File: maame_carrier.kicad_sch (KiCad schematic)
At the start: 30 parts, among them J1 To Kakute H7 V1.5: left strip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, J10 FS-iA10B iBUS servo lead (S +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, J11 TF-Luna pin order 1-6 (CFG ti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, J12 Spare FC I2C (5 V supply, sha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, J13 Payload servo power (+ -); se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, J17 Kakute spare: T3 RSSI 3V3(FC)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, J3 VBAT tap from ESC battery pad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, J4 Micro BEC input leads (6-60 V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, J5 Micro BEC output leads (set t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, J6 Spare power: 5V_AUX G 5V_FC G, J7 Pi expansion: 3V3 logic ONLY, J8 TBS M10Q: order matches its p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, J9 SiK radio (UART4), U1 Raspberry Pi Zero W v1.1, com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

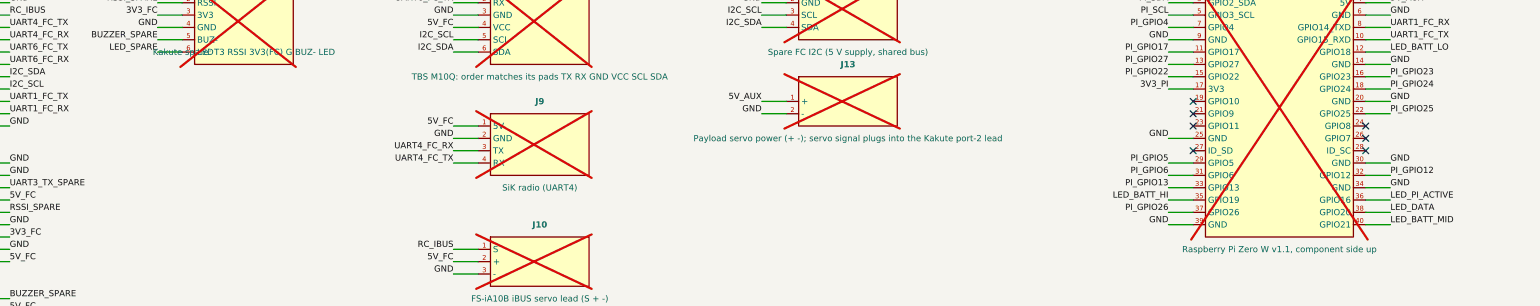
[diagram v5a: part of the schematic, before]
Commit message: J18 Pi SPI header (3V3 GND MOSI MISO SCLK CE0 CE1); re-routed; DRC 0 errors; fab files regenerated
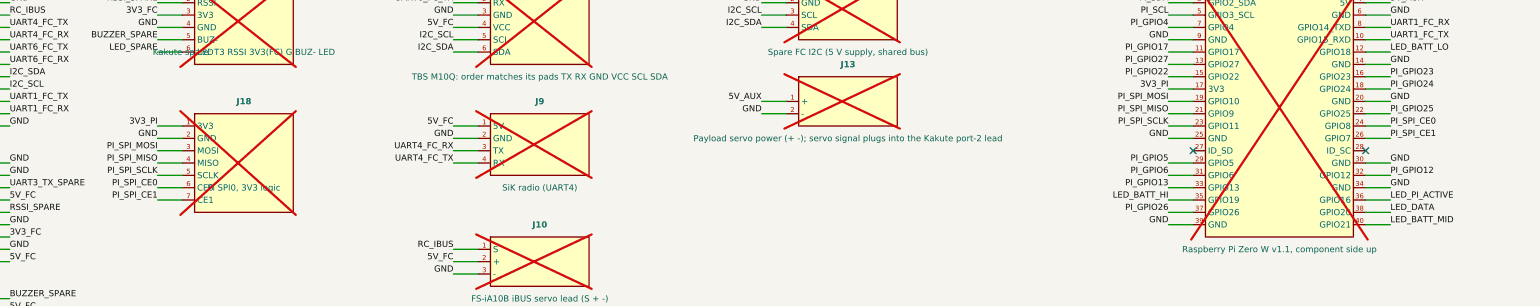
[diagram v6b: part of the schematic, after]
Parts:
- added J18: Pi SPI0, 3V3 logic, Connector_PinHeader_2.54mm:PinHeader_1x07_P2.54mm_Vertical, symbol maame_carrier:PI_SPI
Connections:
- net 3V3_PI: now also J18.1 (3V3)
- net GND: now also J18.2 (GND)
- net PI_SPI_MOSI: now reaches U1.19 (GPIO10)
- net PI_SPI_MOSI: now also J18.3 (MOSI)
- net PI_SPI_MISO: now reaches U1.21 (GPIO9)
- net PI_SPI_MISO: now also J18.4 (MISO)
- net PI_SPI_SCLK: now reaches U1.23 (GPIO11)
- net PI_SPI_SCLK: now also J18.5 (SCLK)
- net PI_SPI_CE0: now reaches U1.24 (GPIO8)
- net PI_SPI_CE0: now also J18.6 (CE0)
- net PI_SPI_CE1: now reaches U1.26 (GPIO7)
- net PI_SPI_CE1: now also J18.7 (CE1)
- no-connect marks 12 -> 7

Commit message: On-board 5V 3.5A buck (TPS54360B, TI Fig.32 values) replaces the external BEC and J4/J5; SW node as copper zone; re-routed, DRC 0 errors; fab files regenerated
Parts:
- removed J4: Micro BEC input leads (6-60 V, NO reverse protect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, Connector_Wire:SolderWire-0.5sqmm_1x02_P4.6mm_D0.9mm_OD2.1mm, symbol maame_carrier:BEC_IN
- removed J5: Micro BEC output leads (set to 5.0 V), Connector_Wire:SolderWire-0.5sqmm_1x02_P4.6mm_D0.9mm_OD2.1mm, symbol maame_carrier:BEC_OUT
- added C2, C3: 2.2uF 100V X7R 1210 (VIN), Capacitor_SMD:C_1210_3225Metric, symbol maame_carrier:Capacitor
- added C4: 100nF 50V 0603 (BOOT), Capacitor_SMD:C_0603_1608Metric, symbol maame_carrier:Capacitor
- added C5: 6.8nF 50V 0603 (COMP), Capacitor_SMD:C_0603_1608Metric, symbol maame_carrier:Capacitor
- added C6, C7: 47uF 10V X7R 1210 (OUT), Capacitor_SMD:C_1210_3225Metric, symbol maame_carrier:Capacitor
- added C8: 39pF 50V C0G 0603 (COMP), Capacitor_SMD:C_0603_1608Metric, symbol maame_carrier:Capacitor
- added D8: B560C 60V 5A Schottky SMC, Diode_SMD:D_SMC, symbol maame_carrier:Schottky
- added L1: 8.2uH 8.4A Coilcraft XAL6060-822MEC, Inductor_SMD:L_Coilcraft_XAL6060-XXX, symbol maame_carrier:Inductor
- added R10: 53.6k 1% 0603 (FB top), Resistor_SMD:R_0603_1608Metric, symbol maame_carrier:Resistor
- added R11: 10k 1% 0603 (FB bottom), Resistor_SMD:R_0603_1608Metric, symbol maame_carrier:Resistor
- added R8: 162k 1% 0603 (RT, 600 kHz), Resistor_SMD:R_0603_1608Metric, symbol maame_carrier:Resistor
- added R9: 13k 1% 0603 (COMP), Resistor_SMD:R_0603_1608Metric, symbol maame_carrier:Resistor
- added U2: TPS54360BDDAR 60V 3.5A buck, Package_SO:TI_SO-PowerPAD-8_ThermalVias, symbol maame_carrier:TPS54360B
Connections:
- net 5V_AUX: now also C6.1, C7.1, L1.2, R10.1
- net GND: now also C2.2, C3.2, C5.2, C6.2, C7.2, C8.2, D8.2 (A), R11.2, R8.2, U2.7 (GND), U2.9 (EP)
- net VBAT_F: now also C2.1, C3.1, U2.2 (VIN)
- new net BEC_BOOT: C4.1, U2.1 (BOOT)
- new net BEC_COMP: C8.1, R9.1, U2.6 (COMP)
- new net BEC_COMP_RC: C5.1, R9.2
- new net BEC_FB: R10.2, R11.1, U2.5 (FB)
- new net BEC_RT: R8.1, U2.4 (RT/CLK)
- new net BEC_SW: C4.2, D8.1 (K), L1.1, U2.8 (SW)
- no-connect marks 7 -> 8
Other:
- note added: "10. On-board 5V_AUX buck replaces the external BEC: TPS54360B per TI SNVSB93 Fig. 32 (600 kHz, 8.2 uH, B560C, 2x47 uF). UVLO divider omitted (EN floats = enabled, internal UVLO 4.3 V); FB 53.6k/10k = 5.09 V. VIN from VBAT_F (after F1)."
- note added: "8. Former micro BEC (now on-board, see note 10): 6-60 V in, 5 V default (9/12 V selectable), 18x15x4.5 mm, 2.54 mm pins. NO reverse-polarity protection. 5 V rated 1.8-2.8 A continuous depending on input voltage (3.5 A for 2 s). 5V_AUX load: Pi Zero W + 9 g payload servo, within 1.8 A. Battery 6S Li-ion (18-25.2 V): BEC input <= 9 W / 18 V / 0.9 = 0.55 A, so F1 ~1.1 A hold has margin; F1 must be r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"
- note removed: "8. Micro BEC (J4 in, J5 out): 6-60 V in, 5 V default (9/12 V selectable), 18x15x4.5 mm, 2.54 mm pins. NO reverse-polarity protection. 5 V rated 1.8-2.8 A continuous depending on input voltage (3.5 A for 2 s). 5V_AUX load: Pi Zero W + 9 g payload servo, within 1.8 A. Battery 6S Li-ion (18-25.2 V): BEC input <= 9 W / 18 V / 0.9 = 0.55 A, so F1 ~1.1 A hold has margin; F1 must be rated >= 30 V (keep 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"

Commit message: F1 -> 2 A hold / 30 V PTC (BSMD1812-200-30V, C960026) so the on-board buck can deliver its full 3.5 A; notes and fab files updated
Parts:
- F1: value PTC fuse 1812 33V 1.1A hold (TECHFUSE mSMD110-33V, LCSC C70119) -> PTC fuse 1812 30V 2A hold 4A trip (BSMD1812-200-30V, LCSC C960026); LCSC C70119 -> C960026
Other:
- note added: "8. Power: 6S Li-ion (18-25.2 V) from J3 tap -> F1 PTC (2 A hold, 4 A trip, 30 V) -> U2 5 V buck (note 10) -> 5V_AUX. Full 3.5 A out at 18 V in draws ~1.1 A."
- note removed: "8. Former micro BEC (now on-board, see note 10): 6-60 V in, 5 V default (9/12 V selectable), 18x15x4.5 mm, 2.54 mm pins. NO reverse-polarity protection. 5 V rated 1.8-2.8 A continuous depending on input voltage (3.5 A for 2 s). 5V_AUX load: Pi Zero W + 9 g payload servo, within 1.8 A. Battery 6S Li-ion (18-25.2 V): BEC input <= 9 W / 18 V / 0.9 = 0.55 A, so F1 ~1.1 A hold has margin; F1 must be r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"
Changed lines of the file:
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@@
 		)
 	)
-	(text "8. Former micro BEC (now on-board, see note 10): 6-60 V in, 5 V default (9/12 V selectable), 18x15x4.5 mm, 2.54 mm pins. NO reverse-polarity protection. 5 V rated 1.8-2.8 A continuous depending on input voltage (3.5 A for 2 s). 5V_AUX load: Pi Zero W + 9 g payload servo, within 1.8 A. Battery 6S Li-ion (18-25.2 V): BEC input <= 9 W / 18 V / 0.9 = 0.55 A, so F1 ~1.1 A hold has margin; F1 must be rated >= 30 V (keep >= 33 V)."
+	(text "8. Power: 6S Li-ion (18-25.2 V) from J3 tap -> F1 PTC (2 A hold, 4 A trip, 30 V) -> U2 5 V buck (note 10) -> 5V_AUX. Full 3.5 A out at 18 V in draws ~1.1 A."
 		(exclude_from_sim no)
 		(at 20.32 294.64 0)
@@
 			)
 		)
-		(property "Value" "PTC fuse 1812 33V 1.1A hold (TECHFUSE mSMD110-33V, LCSC C70119)"
+		(property "Value" "PTC fuse 1812 30V 2A hold 4A trip (BSMD1812-200-30V, LCSC C960026)"
 			(at 101.6 137.16 0)
 			(show_name no)
@@
 			)
 		)
-		(property "LCSC" "C70119"
+		(property "LCSC" "C960026"
 			(at 101.6 132.08 0)
 			(hide yes)
